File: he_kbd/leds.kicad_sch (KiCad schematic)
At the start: 83 parts

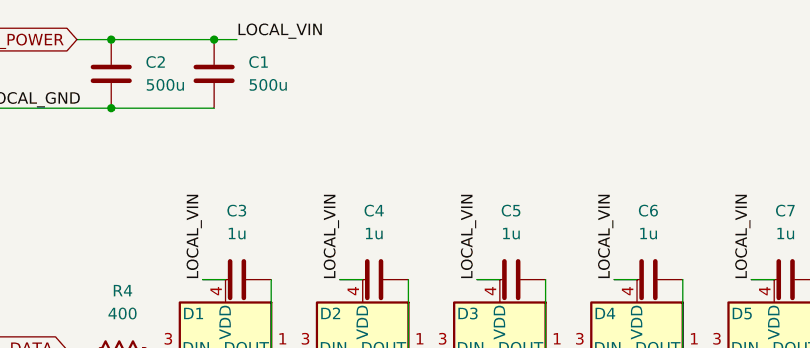
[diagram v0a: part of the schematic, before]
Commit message: fixed up the net classes
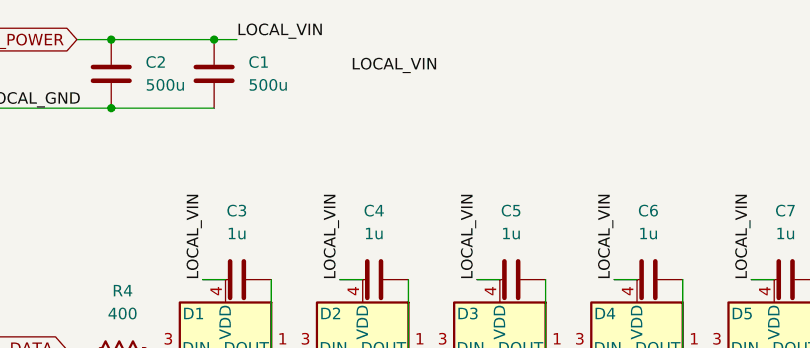
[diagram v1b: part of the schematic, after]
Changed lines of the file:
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@@
+	)
+	(label "LOCAL_VIN"
+		(at 63.5 19.05 0)
+		(fields_autoplaced yes)
+		(effects
+			(font
+				(size 1.27 1.27)
+			)
+			(justify left bottom)
+		)
+		(property "NEOPIXEL_POWER" ""
+			(at 63.5 20.32 0)
+			(show_name yes)
+			(effects
+				(font
+					(size 1.27 1.27)
+					(italic yes)
+				)
+				(justify left)
+			)
+		)
 	)
 	(label "LOCAL_VIN"

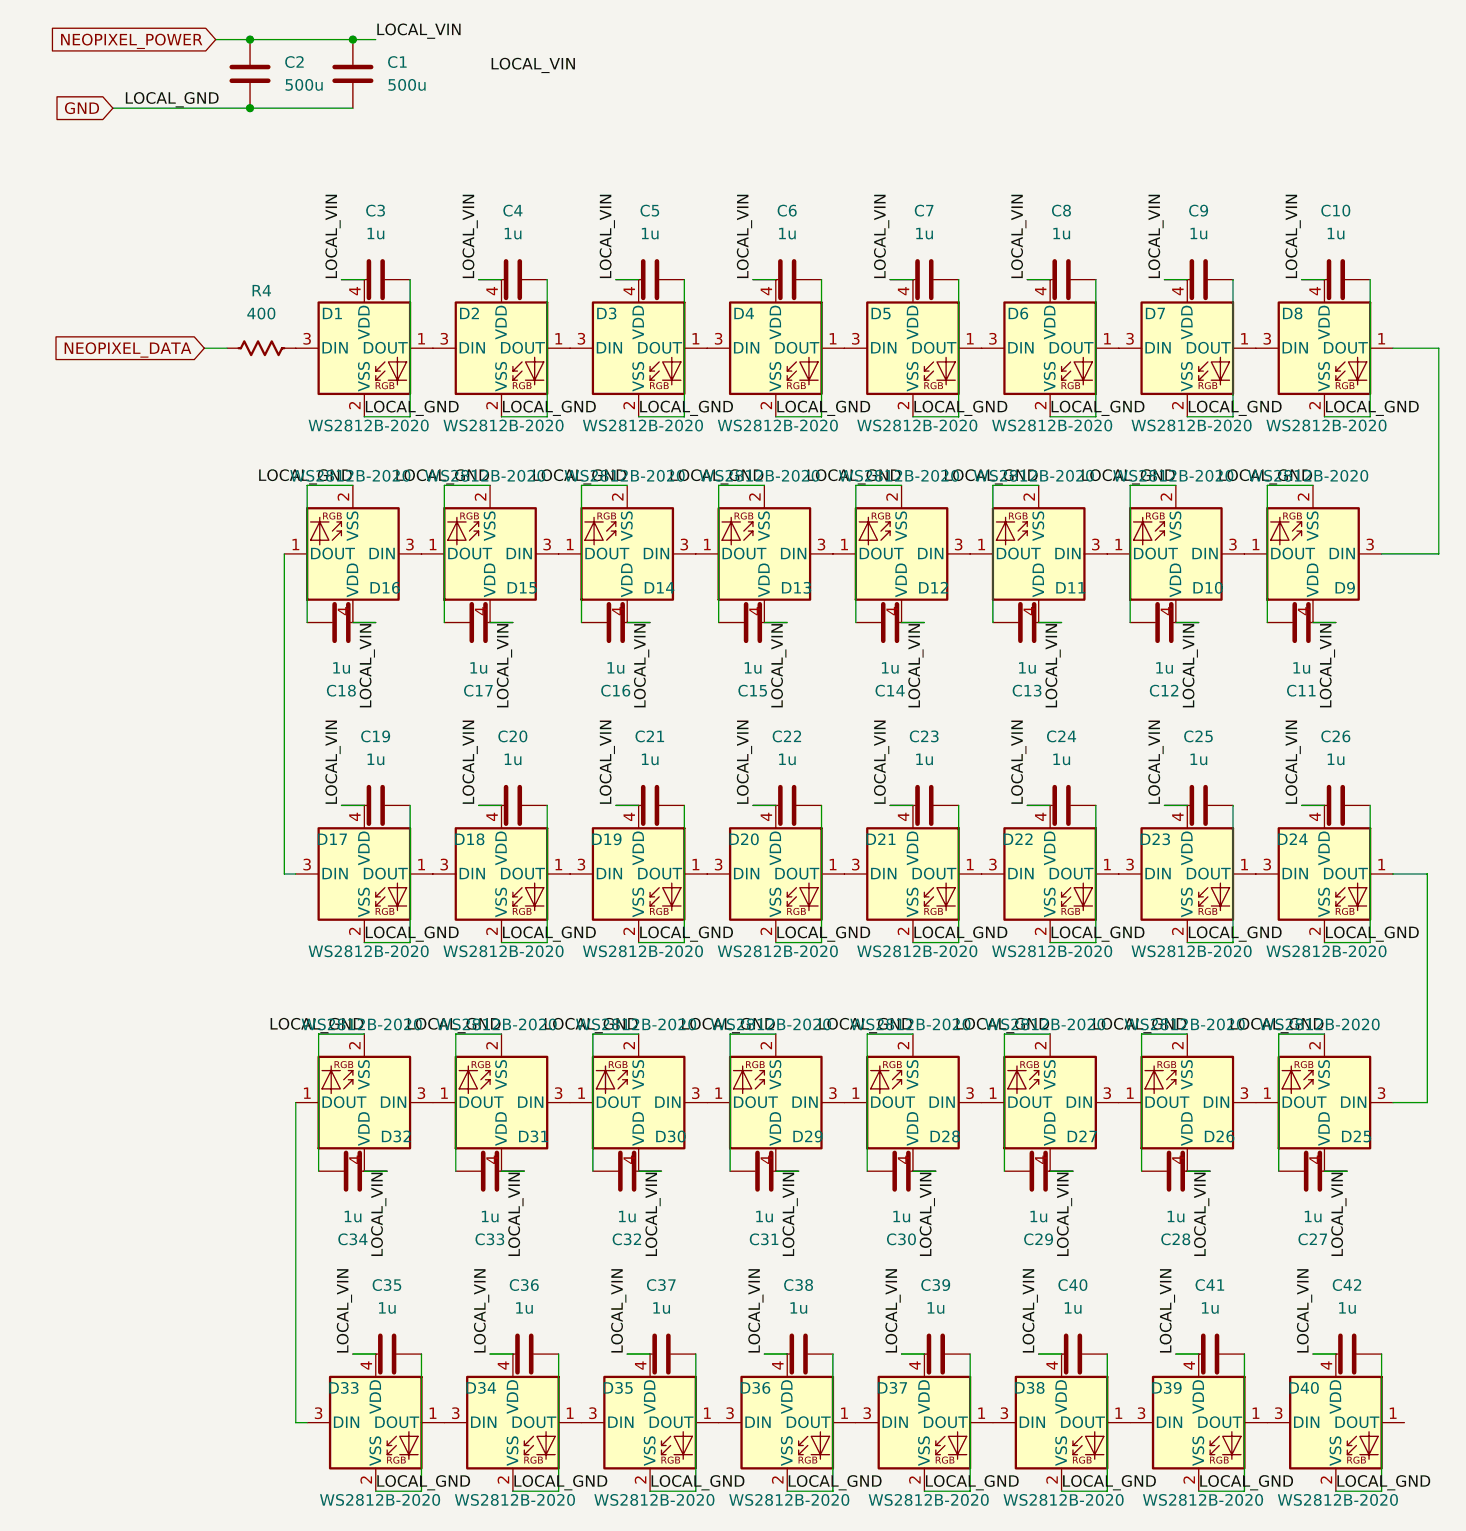
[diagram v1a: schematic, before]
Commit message: before updating pcb files, i added / changed some schematic components
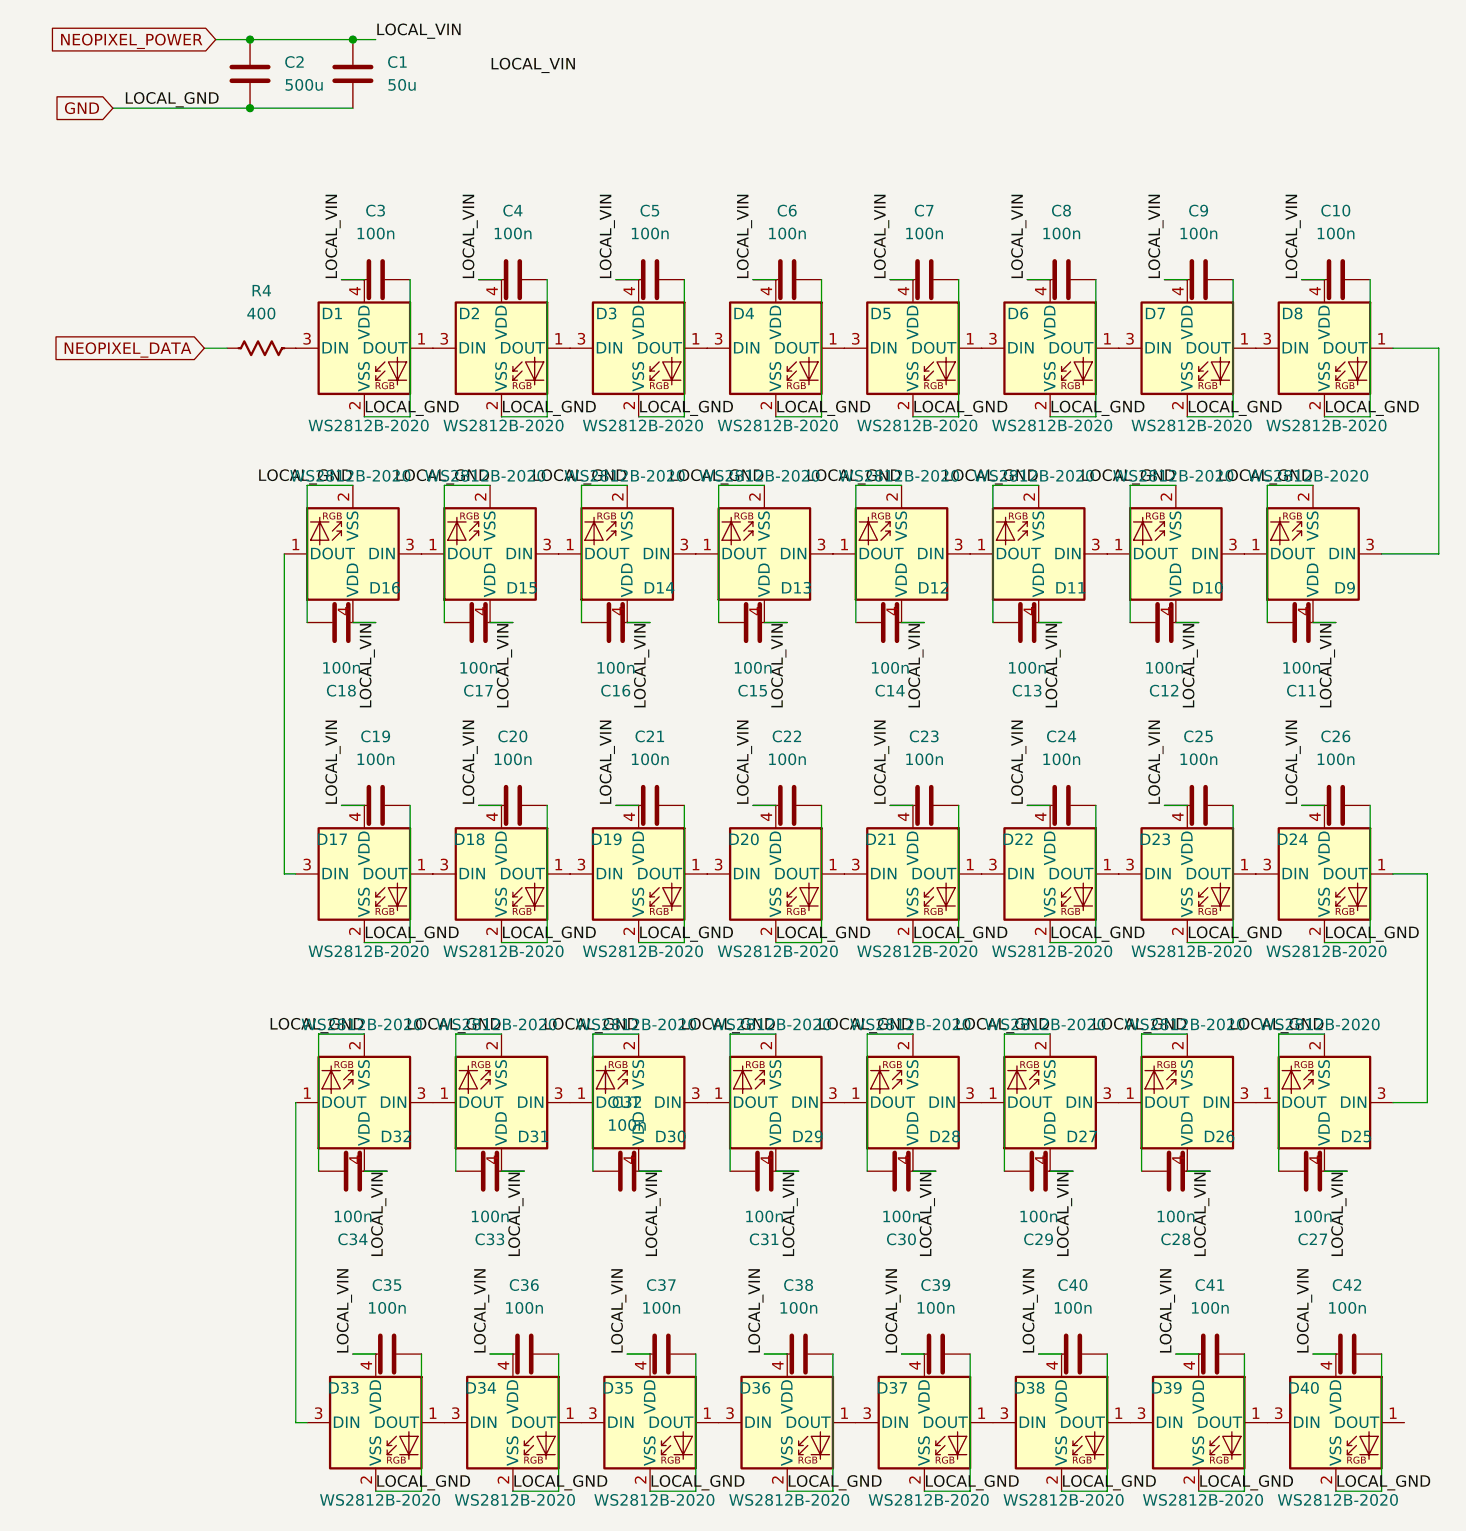
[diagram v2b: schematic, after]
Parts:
- C1: value 500u -> 50u
- C10, C11, C12, C13, C14, C15, C16, C17, C18, C19, C20, C21, C22, C23, C24, C25, C26, C27, C28, C29, C3, C30, C31, C32, C33, C34, C35, C36, C37, C38, C39, C4, C40, C41, C42, C5, C6, C7, C8, C9: value 1u -> 100n
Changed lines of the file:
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@@
 			)
 		)
-		(property "Value" "1u"
+		(property "Value" "100n"
 			(at 157.48 36.83 90)
 			(effects
@@
 			)
 		)
-		(property "Value" "1u"
+		(property "Value" "100n"
 			(at 81.28 95.25 90)
 			(effects
@@
 			)
 		)
-		(property "Value" "1u"
+		(property "Value" "100n"
 			(at 127 36.83 90)
 			(effects
@@
 			)
 		)
-		(property "Value" "1u"
+		(property "Value" "100n"
 			(at 63.5 146.05 90)
 			(effects
@@
 			)
 		)
-		(property "Value" "1u"
+		(property "Value" "100n"
 			(at 153.67 85.09 90)
 			(effects
@@
 			)
 		)
-		(property "Value" "1u"
+		(property "Value" "100n"
 			(at 50.8 36.83 90)
 			(effects
@@
 			)
 		)
-		(property "Value" "1u"
+		(property "Value" "100n"
 			(at 66.04 95.25 90)
 			(effects
@@
 			)
 		)
-		(property "Value" "1u"
+		(property "Value" "100n"
 			(at 50.8 95.25 90)
 			(effects
@@
 			)
 		)
-		(property "Value" "1u"
+		(property "Value" "100n"
 			(at 96.52 36.83 90)
 			(effects
@@
 			)
 		)
-		(property "Value" "1u"
+		(property "Value" "100n"
 			(at 111.76 95.25 90)
 			(effects
@@
 			)
 		)
-		(property "Value" "1u"
+		(property "Value" "100n"
 			(at 127 95.25 90)
 			(effects
@@
 			)
 		)
-		(property "Value" "1u"
+		(property "Value" "100n"
 			(at 111.76 36.83 90)
 			(effects
@@
 			)
 		)
-		(property "Value" "1u"
+		(property "Value" "100n"
 			(at 143.51 156.21 90)
 			(effects
@@
 			)
 		)
-		(property "Value" "1u"
+		(property "Value" "100n"
 			(at 92.71 85.09 90)
 			(effects
@@
 			)
 		)
-		(property "Value" "1u"
+		(property "Value" "100n"
 			(at 142.24 95.25 90)
 			(effects
@@
 			)
 		)
-		(property "Value" "1u"
+		(property "Value" "100n"
 			(at 48.26 146.05 90)
 			(effects
@@
 			)
 		)
-		(property "Value" "1u"
+		(property "Value" "100n"
 			(at 93.98 146.05 90)
 			(effects
@@
 			)
 		)
-		(property "Value" "1u"
+		(property "Value" "100n"
 			(at 96.52 95.25 90)
 			(effects
@@
 			)
 		)
-		(property "Value" "1u"
+		(property "Value" "100n"
 			(at 62.23 85.09 90)
 			(effects
@@
 			)
 		)
-		(property "Value" "1u"
+		(property "Value" "100n"
 			(at 67.31 156.21 90)
 			(effects
@@
 			)
 		)
-		(property "Value" "1u"
+		(property "Value" "100n"
 			(at 107.95 85.09 90)
 			(effects
@@
 			)
 		)
-		(property "Value" "1u"
+		(property "Value" "100n"
 			(at 52.07 156.21 90)
 			(effects
@@
 			)
 		)
-		(property "Value" "1u"
+		(property "Value" "100n"
 			(at 128.27 156.21 90)
 			(effects
@@
 			)
 		)
-		(property "Value" "1u"
+		(property "Value" "100n"
 			(at 142.24 36.83 90)
 			(effects
@@
 			)
 		)
-		(property "Value" "1u"
+		(property "Value" "100n"
 			(at 81.28 36.83 90)
 			(effects
@@
 			)
 		)
-		(property "Value" "1u"
+		(property "Value" "100n"
 			(at 124.46 146.05 90)
 			(effects
@@
 			)
 		)
-		(property "Value" "1u"
+		(property "Value" "100n"
 			(at 139.7 146.05 90)
 			(effects
@@
 			)
 		)
-		(property "Value" "1u"
+		(property "Value" "100n"
 			(at 109.22 146.05 90)
 			(effects
@@
 			)
 		)
-		(property "Value" "1u"
+		(property "Value" "100n"
 			(at 154.94 146.05 90)
 			(effects
@@
 			)
 		)
-		(property "Value" "1u"
+		(property "Value" "100n"
 			(at 82.55 156.21 90)
 			(effects
@@
 			)
 		)
-		(property "Value" "1u"
+		(property "Value" "100n"
 			(at 158.75 156.21 90)
 			(effects
@@
 			)
 		)
-		(property "Value" "1u"
+		(property "Value" "100n"
 			(at 77.47 85.09 90)
 			(effects
@@
 			)
 		)
-		(property "Value" "1u"
+		(property "Value" "100n"
 			(at 138.43 85.09 90)
 			(effects
@@
 			)
 		)
-		(property "Value" "1u"
+		(property "Value" "100n"
 			(at 46.99 85.09 90)
 			(effects
@@
 			)
 		)
-		(property "Value" "1u"
+		(property "Value" "100n"
 			(at 97.79 156.21 90)
 			(effects
@@
 			)
 		)
-		(property "Value" "1u"
+		(property "Value" "100n"
 			(at 66.04 36.83 90)
 			(effects
@@
 			)
 		)
-		(property "Value" "1u"
+		(property "Value" "100n"
 			(at 157.48 95.25 90)
 			(effects
@@
 			)
 		)
-		(property "Value" "500u"
+		(property "Value" "50u"
 			(at 52.07 20.3199 0)
 			(effects
@@
 			)
 		)
-		(property "Value" "1u"
+		(property "Value" "100n"
 			(at 113.03 156.21 90)
 			(effects
@@
 			)
 		)
-		(property "Value" "1u"
+		(property "Value" "100n"
 			(at 123.19 85.09 90)
 			(effects
@@
 		(fields_autoplaced yes)
 		(property "Reference" "C32"
-			(at 78.74 148.59 90)
+			(at 78.74 133.35 90)
 			(effects
 				(font
@@
 			)
 		)
-		(property "Value" "1u"
-			(at 78.74 146.05 90)
+		(property "Value" "100n"
+			(at 78.74 135.89 90)
 			(effects
 				(font

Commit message: more progress
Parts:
- removed C36, C37, C38, C39, C40, C41, C42: 100n, PCM_Capacitor_SMD_AKL:C_0402_1005Metric, symbol PCM_Capacitor_AKL:C_0805
- removed D34, D35, D36, D37, D38, D39, D40: WS2812B-2020, LED_SMD:LED_WS2812B-2020_PLCC4_2.0x2.0mm, symbol LED:WS2812B-2020

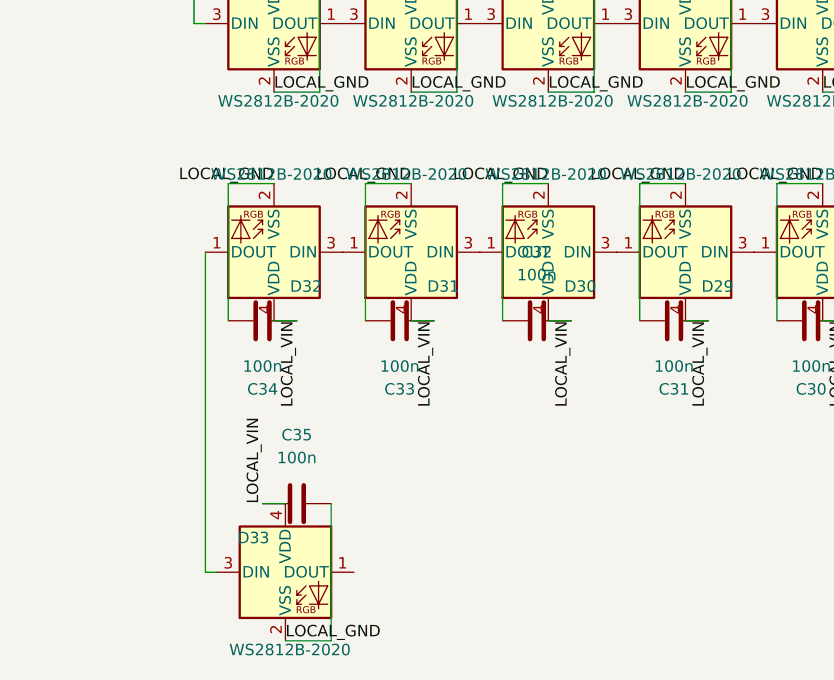
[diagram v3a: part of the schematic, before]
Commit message: realised have to change capacitor footprint entirely
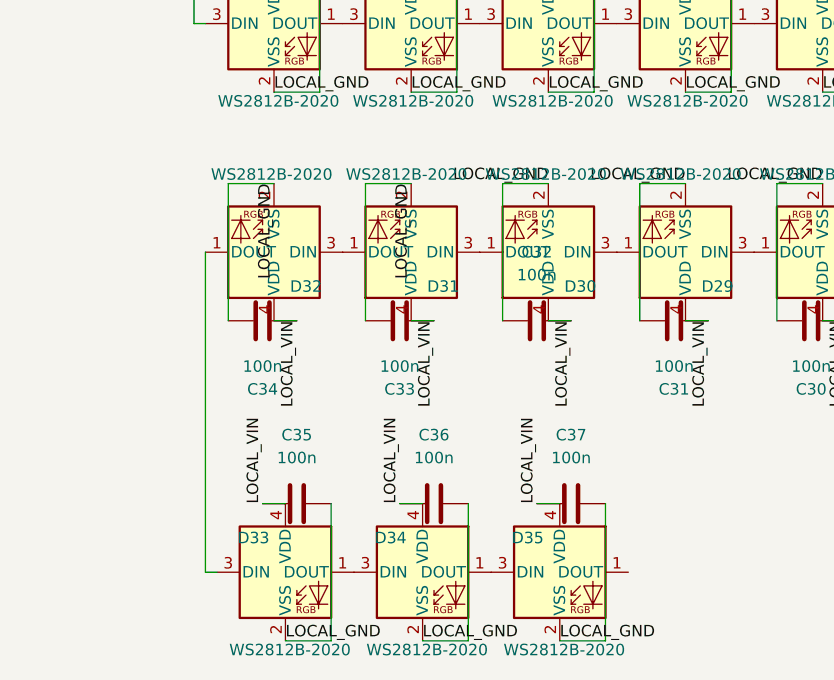
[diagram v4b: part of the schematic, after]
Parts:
- added C36, C37: 100n, PCM_Capacitor_SMD_AKL:C_0805_2012Metric_Pad1.18x1.45mm_HandSolder, symbol PCM_Capacitor_AKL:C_0805
- added D34, D35: WS2812B-2020, LED_SMD:LED_WS2812B-2020_PLCC4_2.0x2.0mm, symbol LED:WS2812B-2020
- C10, C11, C12, C13, C14, C15, C16, C17, C18, C19, C20, C21, C22, C23, C24, C25, C26, C27, C28, C29, C3, C30, C31, C32, C33, C34, C35, C4, C5, C6, C7, C8, C9: footprint PCM_Capacitor_SMD_AKL:C_0402_1005Metric -> PCM_Capacitor_SMD_AKL:C_0805_2012Metric_Pad1.18x1.45mm_HandSolder
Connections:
- net GND: now also C36.2, C37.2, D34.2 (VSS), D35.2 (VSS)
- net NEOPIXEL_POWER: now also C36.1, C37.1, D34.4 (VDD), D35.4 (VDD)
- net at D33.1 (DOUT): now also D34.3 (DIN)
- new net: D34.1 (DOUT), D35.3 (DIN)

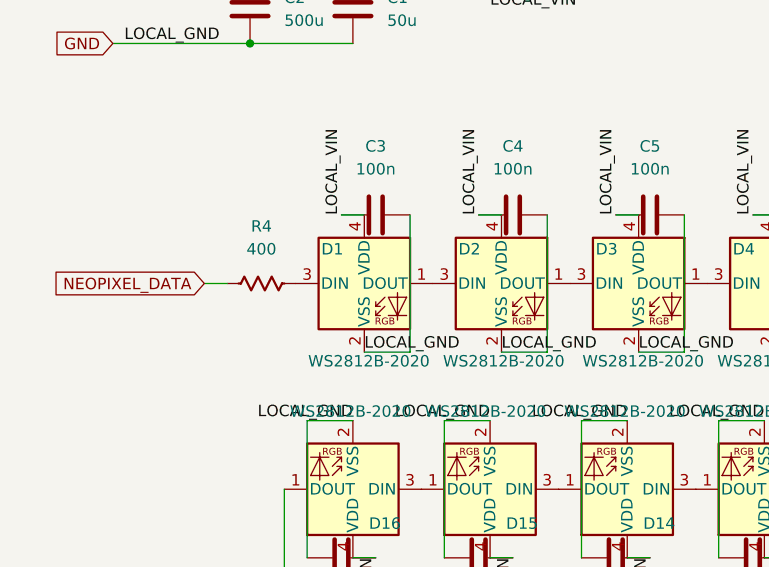
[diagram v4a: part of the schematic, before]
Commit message: i will have to change the led footprint as well lets go
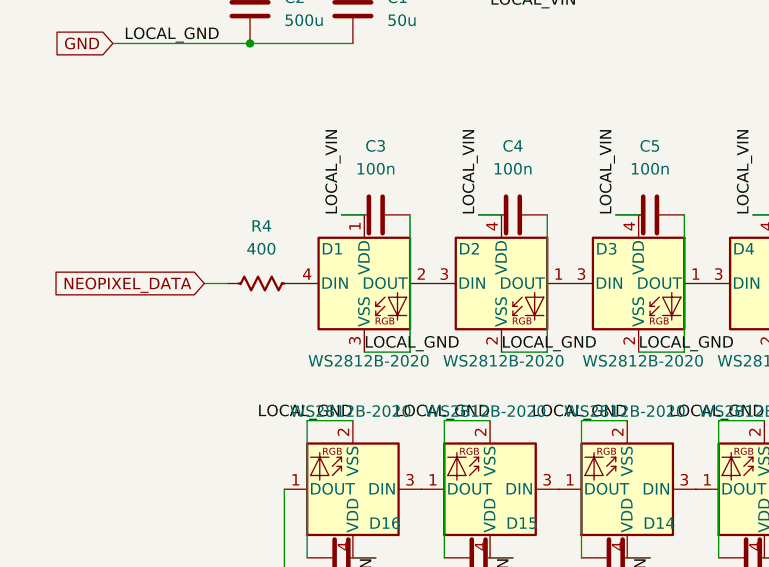
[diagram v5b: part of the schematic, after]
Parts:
- D1: footprint LED_SMD:LED_WS2812B-2020_PLCC4_2.0x2.0mm -> LED_SMD:LED_WS2812B_PLCC4_5.0x5.0mm_P3.2mm; symbol LED:WS2812B-2020 -> LED:WS2812B
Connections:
- net GND: now also D1.3 (VSS); no longer D1.2 (VSS)
- net NEOPIXEL_POWER: now also D1.1 (VDD); no longer D1.4 (VDD)
- net at D2.3 (DIN): now also D1.2 (DOUT); no longer D1.1 (DOUT)
- net at R4.1: now also D1.4 (DIN); no longer D1.3 (DIN)
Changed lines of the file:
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@@
 	)
 	(symbol
-		(lib_id "LED:WS2812B-2020")
+		(lib_id "LED:WS2812B")
 		(at 49.53 49.53 0)
 		(unit 1)
@@
 			)
 		)
-		(property "Footprint" "LED_SMD:LED_WS2812B-2020_PLCC4_2.0x2.0mm"
+		(property "Footprint" "LED_SMD:LED_WS2812B_PLCC4_5.0x5.0mm_P3.2mm"
 			(at 50.8 57.15 0)
 			(effects
@@
 			)
 		)
-		(property "Datasheet" "https://cdn-shop.adafruit.com/product-files/4684/4684_WS2812B-2020_V1.3_EN.pdf"
+		(property "Datasheet" "https://cdn-shop.adafruit.com/datasheets/WS2812B.pdf"
 			(at 52.07 59.055 0)
 			(effects
@@
 			)
 		)
-		(property "Description" "RGB LED with integrated controller, 2.0 x 2.0 mm, 12 mA"
+		(property "Description" "RGB LED with integrated controller"
 			(at 49.53 49.53 0)
 			(effects
